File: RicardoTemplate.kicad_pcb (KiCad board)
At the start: 4 copper layers, 77 parts, among them J1 RBUS, J2 USB_C_Receptacle_USB2.0, U1 ESP32-S3, U2 SN65HVD230, U5 LM66100, U6 LM66100, U7 MAX77827AEFD+T, U8 SC4215, Y1 40MHz±10ppm

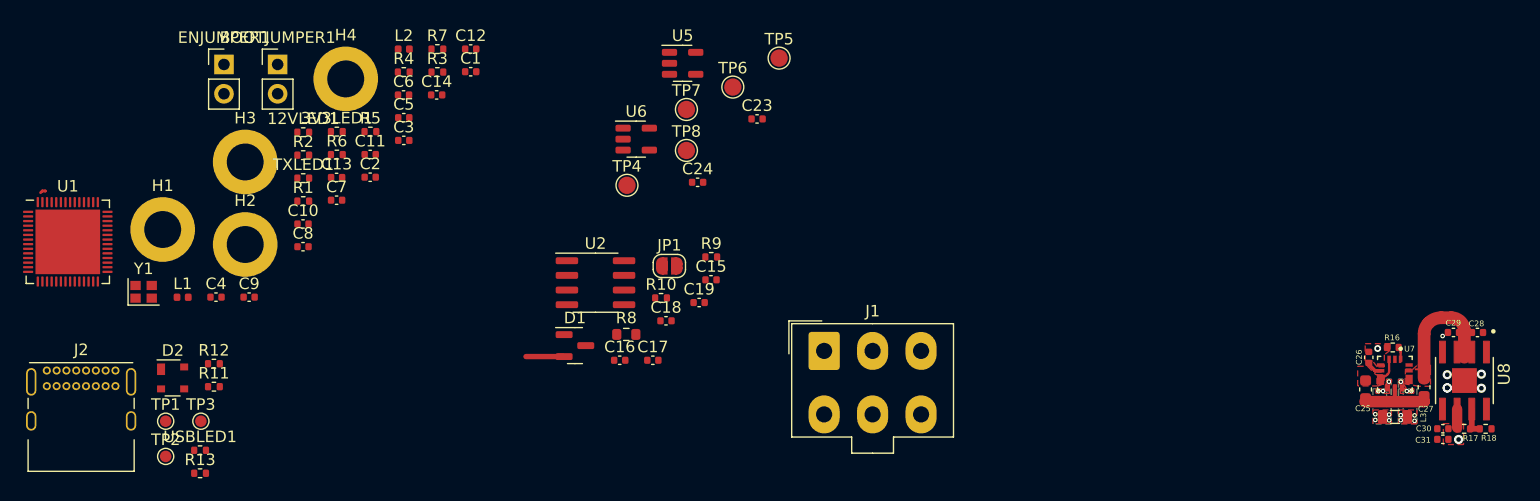
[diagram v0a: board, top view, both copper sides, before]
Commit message: updated ideal oring diode and layout
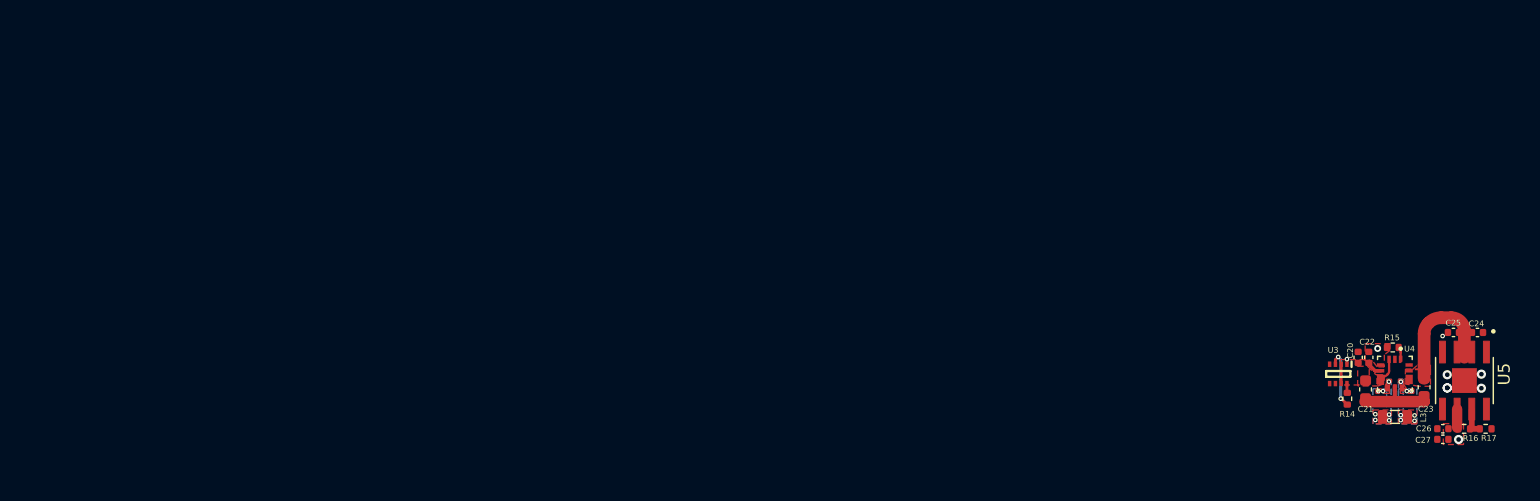
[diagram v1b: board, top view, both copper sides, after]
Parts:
- removed 12VLED1: 12V_LED, Resistor_SMD:R_0402_1005Metric
- removed 3V3LED1: 3V3LED, Resistor_SMD:R_0402_1005Metric
- removed BOOTJUMPER1, ENJUMPER1: Conn_01x02_Male, Connector_PinHeader_2.54mm:PinHeader_1x02_P2.54mm_Vertical
- removed C1, C16: 10uF, Capacitor_SMD:C_0402_1005Metric
- removed C10, C11, C17, C3, C5, C6, C8: 0.1uF, Capacitor_SMD:C_0402_1005Metric
- removed C12: 4.2pF, Capacitor_SMD:C_0402_1005Metric
- removed C13, C14: C, Capacitor_SMD:C_0402_1005Metric
- removed C15: 100nF, Capacitor_SMD:C_0402_1005Metric
- removed C18, C19: 220pF, Capacitor_SMD:C_0402_1005Metric
- removed C2, C4, C7: 1uF, Capacitor_SMD:C_0402_1005Metric
- removed the C23 at (117.7, 64.9)
- removed the C24 at (112.5, 70.4)
- removed C9: 10nF, Capacitor_SMD:C_0402_1005Metric
- removed D1: SM712_SOT23, Package_TO_SOT_SMD:SOT-23
- removed D2: SP0503BAHT, Package_TO_SOT_SMD:SOT-143
- removed H1, H2, H3, H4: MountingHole_Pad, MountingHole:MountingHole_3.2mm_M3_DIN965_Pad
- removed J1: RBUS, Connector_Molex:Molex_Mini-Fit_Jr_5566-06A_2x03_P4.20mm_Vertical
- removed J2: USB_C_Receptacle_USB2.0, Connector_USB:USB_C_Receptacle_GCT_USB4085
- removed JP1: TermJP, Jumper:SolderJumper-2_P1.3mm_Open_RoundedPad1.0x1.5mm
- removed L1: 2.0nH, Inductor_SMD:L_0402_1005Metric
- removed L2: 20nH, Inductor_SMD:L_0402_1005Metric
- removed R1, R3: 10K, Resistor_SMD:R_0402_1005Metric
- removed R10, R9: 60, Resistor_SMD:R_0402_1005Metric
- removed R11, R12: 5.1k, Resistor_SMD:R_0402_1005Metric
- removed R13, R2, R4: 470, Resistor_SMD:R_0402_1005Metric
- removed R5: 47.5, Resistor_SMD:R_0402_1005Metric
- removed R6: 499, Resistor_SMD:R_0402_1005Metric
- removed R7: 3k, Resistor_SMD:R_0402_1005Metric
- removed R8: 0, Resistor_SMD:R_0603_1608Metric
- removed TP1, TP2, TP3: TestPoint, TestPoint:TestPoint_Pad_D1.0mm
- removed TP4, TP5, TP6, TP7, TP8: TestPoint, TestPoint:TestPoint_Pad_D1.5mm
- removed TXLED1: TX_LED, Resistor_SMD:R_0402_1005Metric
- removed U1: ESP32-S3, Package_DFN_QFN:QFN-56-1EP_7x7mm_P0.4mm_EP5.6x5.6mm
- removed U2: SN65HVD230, Package_SO:SOIC-8_3.9x4.9mm_P1.27mm
- removed the U5 at (111.2, 60.1)
- removed U6: LM66100, Package_TO_SOT_SMD:SOT-23-5
- removed USBLED1: USB_LED, Resistor_SMD:R_0402_1005Metric
- removed Y1: 40MHz±10ppm, Crystal:Crystal_SMD_2016-4Pin_2.0x1.6mm
- added C20: 10uF, Capacitor_SMD:C_0402_1005Metric, F.Cu at (169.8, 85.6)
- added R14: 10k, Resistor_SMD:R_0402_1005Metric, F.Cu at (168.8, 89.2)
- added U3: LM66200DRLR, iclr:SOTFL50P160X60-8N, F.Cu at (168.1, 87.0)
- renumbered C25 to C21, C26 to C22, C27 to C23, C28 to C24, C29 to C25, C30 to C26, C31 to C27, R16 to R15, R17 to R16, R18 to R17, U7 to U4, U8 to U5
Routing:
- net VBUS: track 0.00 -> 5.27 mm, vias 0 -> 2
- net /CAN+: track 3.30 -> 0.00 mm
- net /Power/BBIN: track 2.00 -> 3.68 mm
- net Net-(R14-Pad2): track 0.00 -> 0.81 mm
- net GND: track 6.29 -> 6.73 mm, vias 7 -> 8
